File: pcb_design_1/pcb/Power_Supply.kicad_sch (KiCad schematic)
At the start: 0 parts

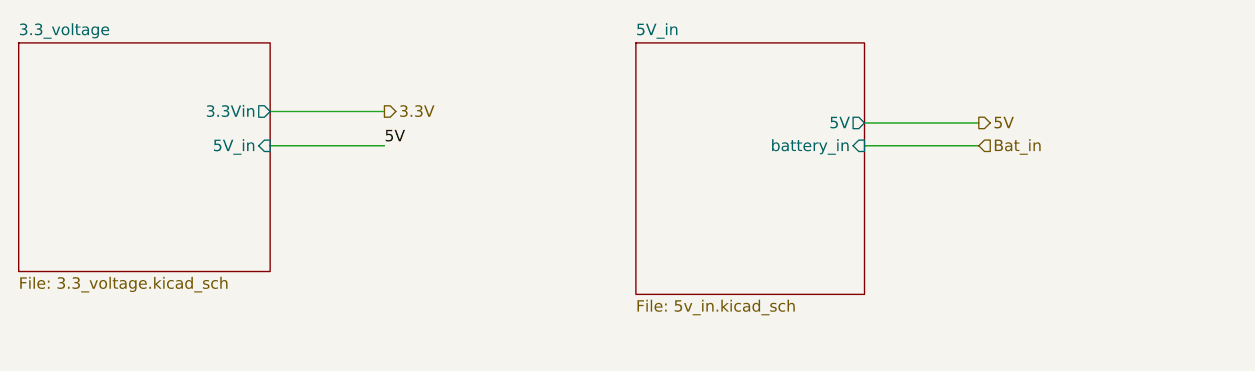
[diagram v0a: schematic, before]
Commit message: Add OLED Display and power switch, rename battery input
Added new OLED Display schematic sheet with I2C connector (J14) and pinout. Integrated OLED display connections (VCC, GND, SDA, SCL) into main PCB. Added power switch (SW1) between battery input and power supply. Renamed battery input signal from 'battery_in' to 'battery_in_1' throughout 5V input and power supply sheets. Updated component designators and repositioned schematic sheets for improved layout organization.
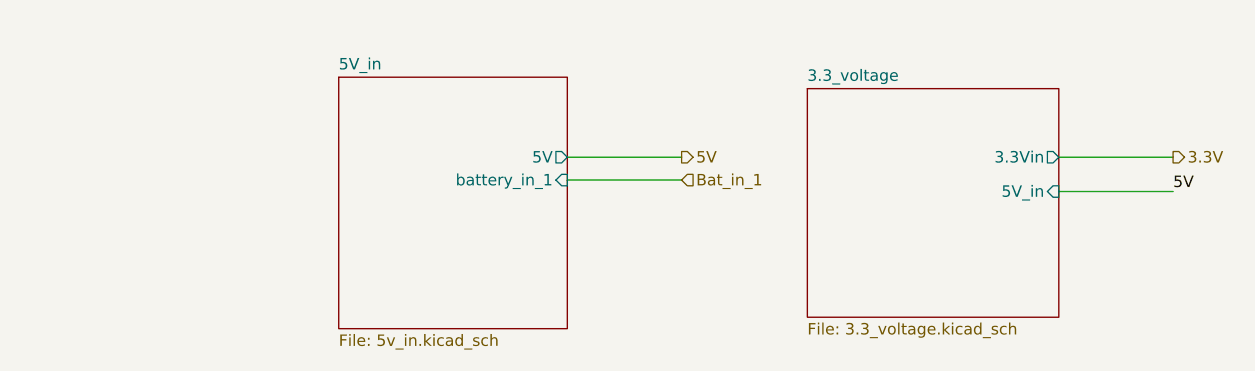
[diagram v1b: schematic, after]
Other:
- sheet 5V_in ports: added battery_in_1; removed battery_in
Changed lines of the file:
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@@
 	(wire
 		(pts
-			(xy 95.25 81.28) (xy 107.95 81.28)
+			(xy 182.88 86.36) (xy 195.58 86.36)
 		)
 		(stroke
@@
 	(wire
 		(pts
-			(xy 95.25 85.09) (xy 107.95 85.09)
+			(xy 182.88 90.17) (xy 195.58 90.17)
 		)
 		(stroke
@@
 	(wire
 		(pts
-			(xy 161.29 82.55) (xy 173.99 82.55)
+			(xy 128.27 86.36) (xy 140.97 86.36)
 		)
 		(stroke
@@
 	(wire
 		(pts
-			(xy 161.29 85.09) (xy 173.99 85.09)
+			(xy 128.27 88.9) (xy 140.97 88.9)
 		)
 		(stroke
@@
 	)
 	(label "5V"
-		(at 107.95 85.09 0)
+		(at 195.58 90.17 0)
 		(effects
 			(font
@@
 	(hierarchical_label "3.3V"
 		(shape output)
-		(at 107.95 81.28 0)
+		(at 195.58 86.36 0)
 		(effects
 			(font
@@
 		)
 	)
-	(hierarchical_label "Bat_in"
+	(hierarchical_label "Bat_in_1"
 		(shape input)
-		(at 173.99 85.09 0)
+		(at 140.97 88.9 0)
 		(effects
 			(font
@@
 	(hierarchical_label "5V"
 		(shape output)
-		(at 173.99 82.55 0)
+		(at 140.97 86.36 0)
 		(effects
 			(font
@@
 	)
 	(sheet
-		(at 135.89 73.66)
+		(at 102.87 77.47)
 		(size 25.4 27.94)
 		(exclude_from_sim no)
@@
 		)
 		(property "Sheetname" "5V_in"
-			(at 135.89 72.9484 0)
+			(at 102.87 76.7584 0)
 			(show_name no)
 			(do_not_autoplace no)
@@
 		)
 		(property "Sheetfile" "5v_in.kicad_sch"
-			(at 135.89 102.1846 0)
+			(at 102.87 105.9946 0)
 			(show_name no)
 			(do_not_autoplace no)
@@
 		)
 		(pin "5V" output
-			(at 161.29 82.55 0)
+			(at 128.27 86.36 0)
 			(effects
 				(font
@@
 			)
 		)
-		(pin "battery_in" input
-			(at 161.29 85.09 0)
+		(pin "battery_in_1" input
+			(at 128.27 88.9 0)
 			(effects
 				(font
@@
 	)
 	(sheet
-		(at 67.31 73.66)
+		(at 154.94 78.74)
 		(size 27.94 25.4)
 		(exclude_from_sim no)
@@
 		)
 		(property "Sheetname" "3.3_voltage"
-			(at 67.31 72.9484 0)
+			(at 154.94 78.0284 0)
 			(show_name no)
 			(do_not_autoplace no)
@@
 		)
 		(property "Sheetfile" "3.3_voltage.kicad_sch"
-			(at 67.31 99.6446 0)
+			(at 154.94 104.7246 0)
 			(show_name no)
 			(do_not_autoplace no)
@@
 		)
 		(pin "3.3Vin" output
-			(at 95.25 81.28 0)
+			(at 182.88 86.36 0)
 			(effects
 				(font
@@
 		)
 		(pin "5V_in" input
-			(at 95.25 85.09 0)
+			(at 182.88 90.17 0)
 			(effects
 				(font
